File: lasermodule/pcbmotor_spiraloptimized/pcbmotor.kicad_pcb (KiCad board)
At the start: 4 copper layers, 45.5 x 43.4 mm, 4 parts, among them J1 Conn_01x03, J2 Conn_01x01, J3 Conn_01x01, J4 Conn_01x01

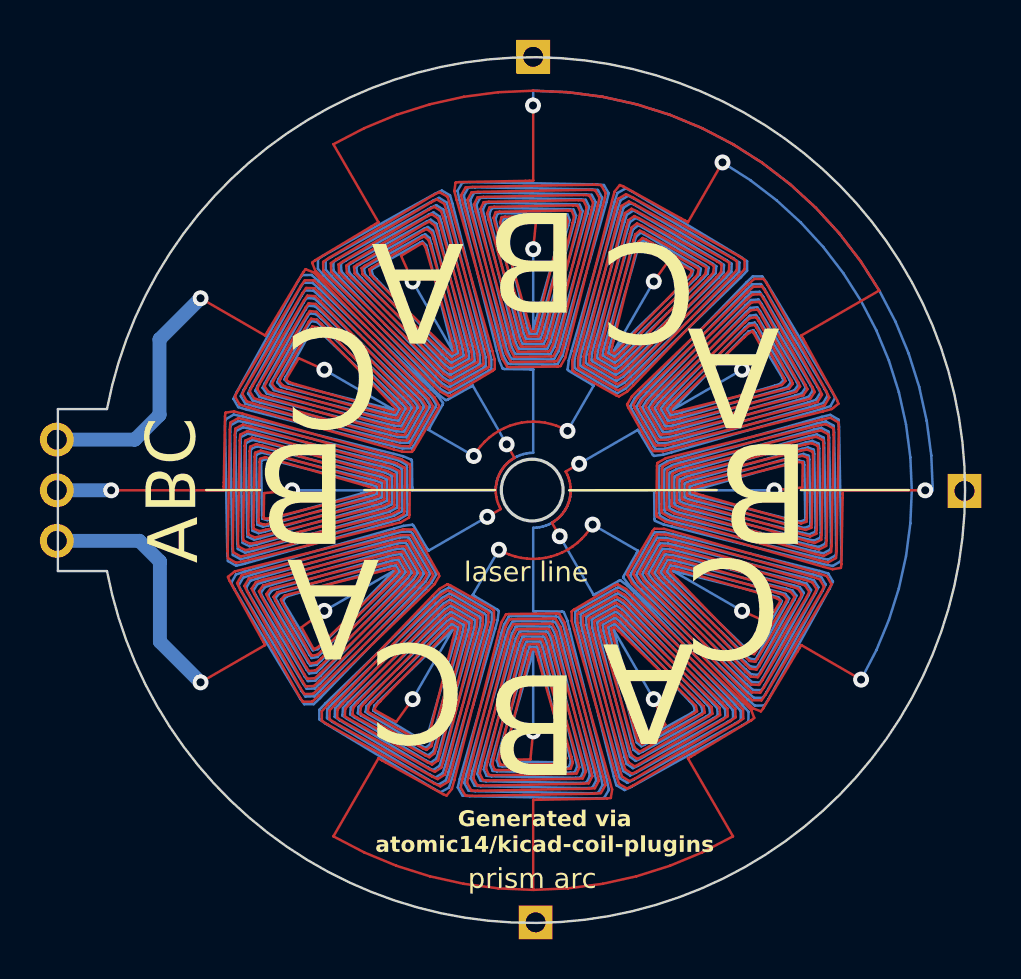
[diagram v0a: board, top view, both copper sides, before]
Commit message: removed need for screws using pcb pads
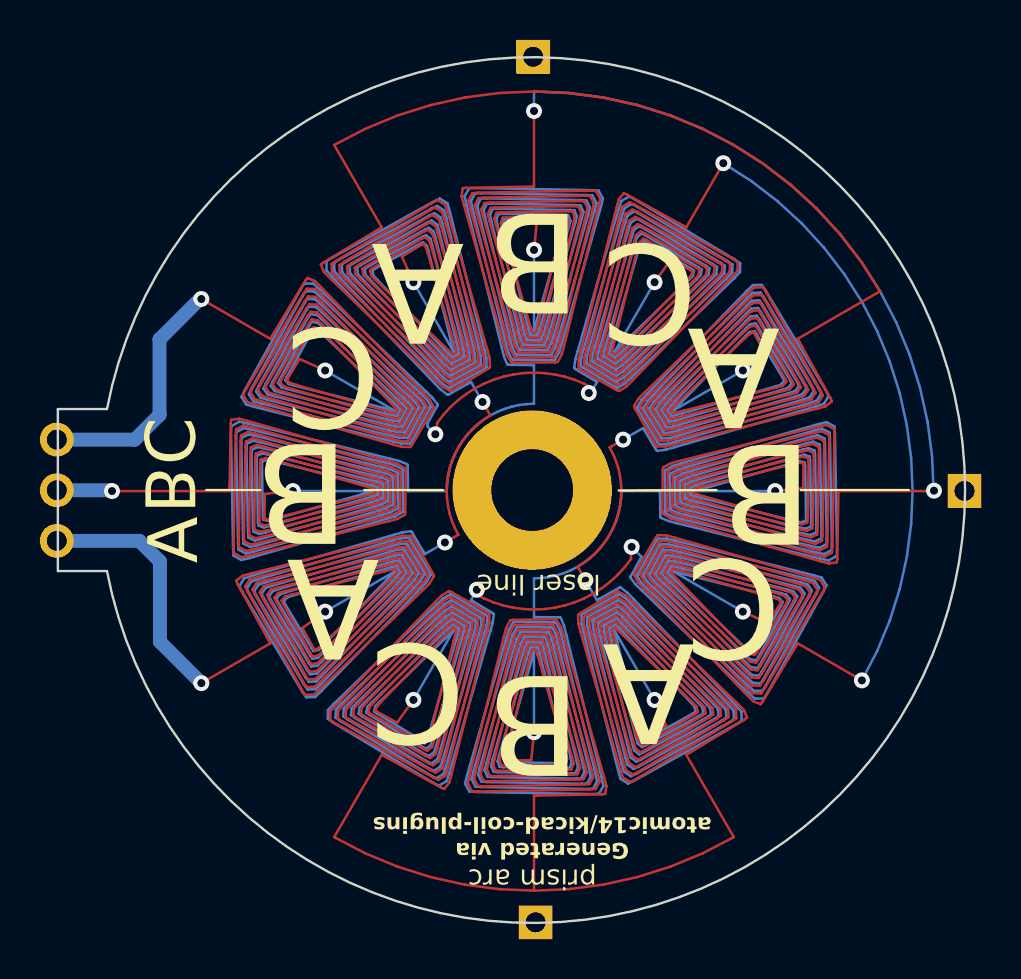
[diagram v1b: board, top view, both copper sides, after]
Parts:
- added J5: Conn_01x01, pcbmotor:motorconnector_D8.0mm_Drill4.1mm, F.Cu at (104.8, 114.1)
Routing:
- net PH1: track 9019.2 -> 7628.7 mm
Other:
- outline, holes or cut-outs redrawn
